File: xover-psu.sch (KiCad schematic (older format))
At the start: 46 parts, among them J1 Screw_Terminal_01x02, J2 Screw_Terminal_01x02, J3 Screw_Terminal_01x02, J4 Screw_Terminal_01x03, J5 Screw_Terminal_01x03, K1 RTE2xxxx, U1 LM317_3PinPackage, U2 LM337_TO220

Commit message: Added unmute-timing draft schematic (mostly FETs, untested)
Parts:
- removed K1: RTE2xxxx, Relay_THT:Relay_DPDT_Schrack-RT2-FormC_RM5mm, symbol Relay:RTE2xxxx
- added C1, C2: 100n, Capacitors_ThroughHole:C_Rect_L18.0mm_W6.0mm_P15.00mm_FKS3_FKP3, symbol Device:C
- added C11, C12: 1000u, Capacitors_ThroughHole:CP_Radial_D16.0mm_P7.50mm, symbol Device:CP
- added C15: 10u, Capacitors_SMD:C_0805, symbol Device:C
- added C3: 220u, Capacitors_SMD:CP_Elec_10x10, symbol Device:C
- added C4: 1u, Capacitors_SMD:C_0805, symbol Device:C
- added D1, D10, D23, D3, D5: LL4148, Diodes_SMD:D_MiniMELF, symbol Device:D
- added D11, D12, D15: M7, Diodes_SMD:D_SMA, symbol Device:D
- added D2, D20, D21, D22, D4: LED, LEDs:LED_0805, symbol Device:LED
- added F1, F2: 500mA, symbol Device:Fuse_Small
- added J2, J6, J7: Screw_Terminal_01x02, Terminals_Phoenix:TerminalBlock_Phoenix_MPT-2.54mm_2pol, symbol Connector:Screw_Terminal_01x02
- added K1: T9GS5L14-12, symbol Relay:RAYEX-L90S
- added L1: PM3700_70_RC, symbol Device:L_Coupled
- added PS1: HLK-10M12, Converter_ACDC:Converter_ACDC_HiLink_HLK-PMxx, symbol Converter_ACDC:HLK-PM12
- added Q1, Q5: AO3400, TO_SOT_Packages_SMD:SOT-23, symbol Device:Q_NMOS_GSD
- added Q2, Q3, Q4: 2N7002, TO_SOT_Packages_SMD:SOT-23, symbol Device:Q_NMOS_GSD
- added R1, R2, R20, R22, R24, R25, R5: 3k9, Resistors_SMD:R_0805, symbol Device:R
- added R10, R6: 47k, Resistors_SMD:R_0805, symbol Device:R
- added R11, R17: 470k, Resistors_SMD:R_0805, symbol Device:R
- added R12: 1k, Resistors_SMD:R_0805, symbol Device:R
- added R21, R3: 100, Resistors_SMD:R_0805, symbol Device:R
- added R23, R4, R7: 10k, Resistors_SMD:R_0805, symbol Device:R
- added RV1, RV2: 10D471K, Varistors:RV_Disc_D12_W3.9_P7.5, symbol Device:Varistor
- added U1, U4: 817C, Package_DIP:DIP-4_W7.62mm, symbol Isolator:PC817
- gave numbers to parts that had none: 2
- renumbered C6 to C10, C7 to C13, C8 to C14, C9 to C16, C10 to C17, C11 to C18, C12 to C19, C13 to C20, C14 to C21, C15 to C22, C16 to C23, C1 to C5, C2 to C6, C3 to C7, C4 to C8, C5 to C9, D5 to D13, D6 to D14, D7 to D16, D8 to D17, D9 to D18, D10 to D19, D1 to D6, D2 to D7, D3 to D8, D4 to D9, J2 to J3, J3 to J4, J4 to J5, J5 to J8, R1 to R13, R2 to R14, R3 to R15, R4 to R16, R5 to R18, R6 to R19, U1 to U2, U2 to U3
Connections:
- net labels added: 12V, AC1, AC2, AGND, DGND, RECT1, VCC, VEE
- net labels removed: GND
- wire segments 180 -> 331
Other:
- note added: "DC Control Supply\nAlways On"
- note added: "Line"
- note added: "Regulated\nOutput\n"
- note added: "Relay"
- note added: "Relay driver on 12V control supply"
- note added: "Remote"
- note added: "Turn-on Delay with Reset\n1s rise-time, fast turn-off\n"
- note added: "Turnoff-Detection\nFast Rise, 100ms fall"
- note added: "Unmute"
- note removed: "DC"
- note removed: "HV AC"
- note removed: "LV AC"
- note removed: "Remote On 12V"
- moved on the sheet: C13, C14, C16, C17, C18, C19, C20, C21, C22, C23, D13, D14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

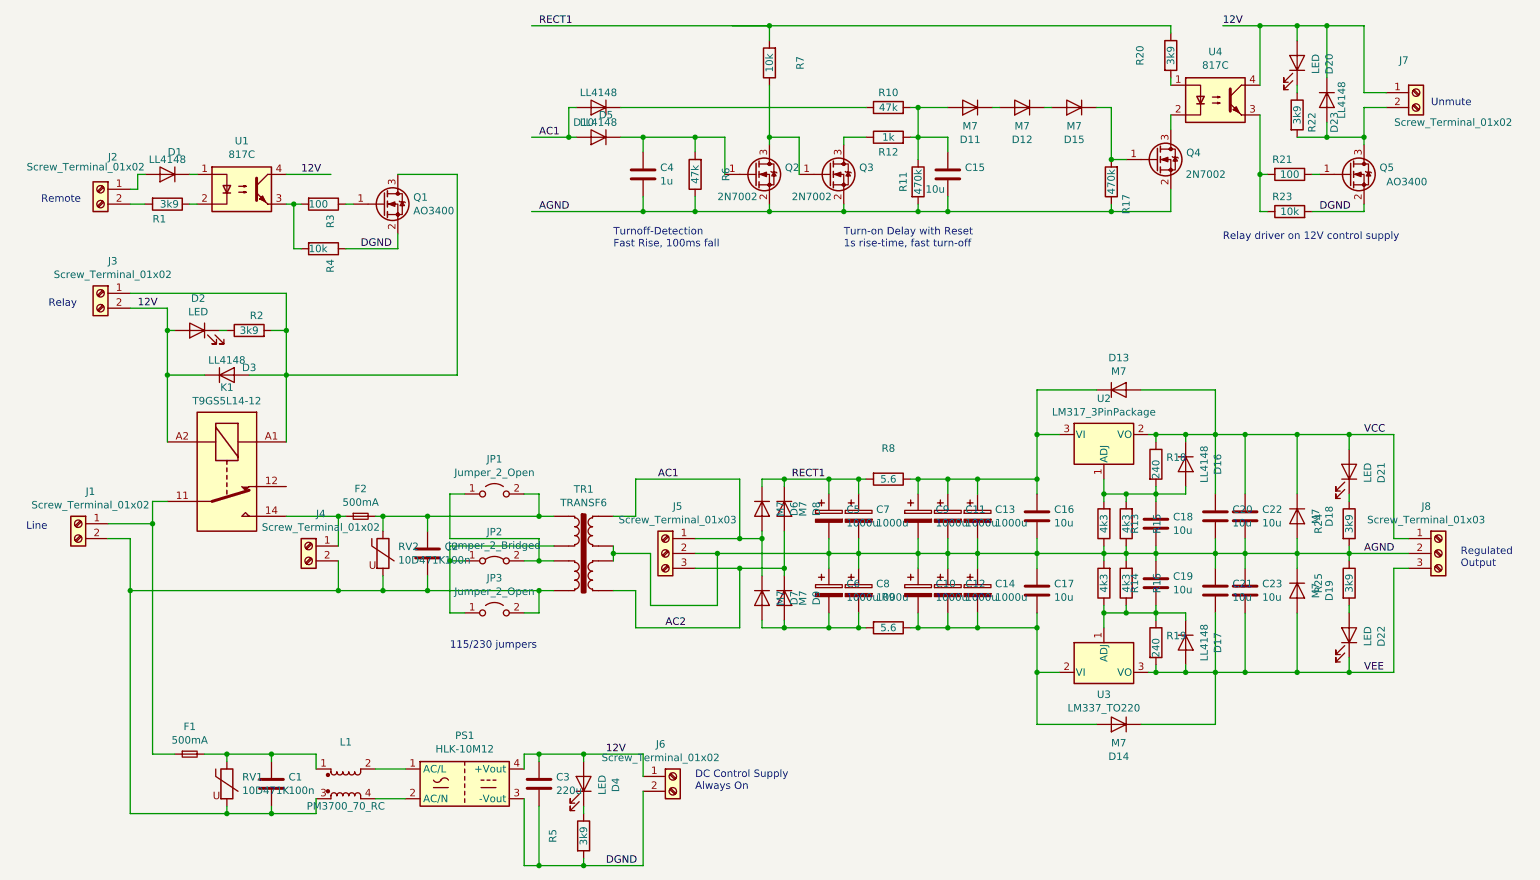
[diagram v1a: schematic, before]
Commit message: Converted unmute circuit to TL431 for distinct turn-on/off behaviour
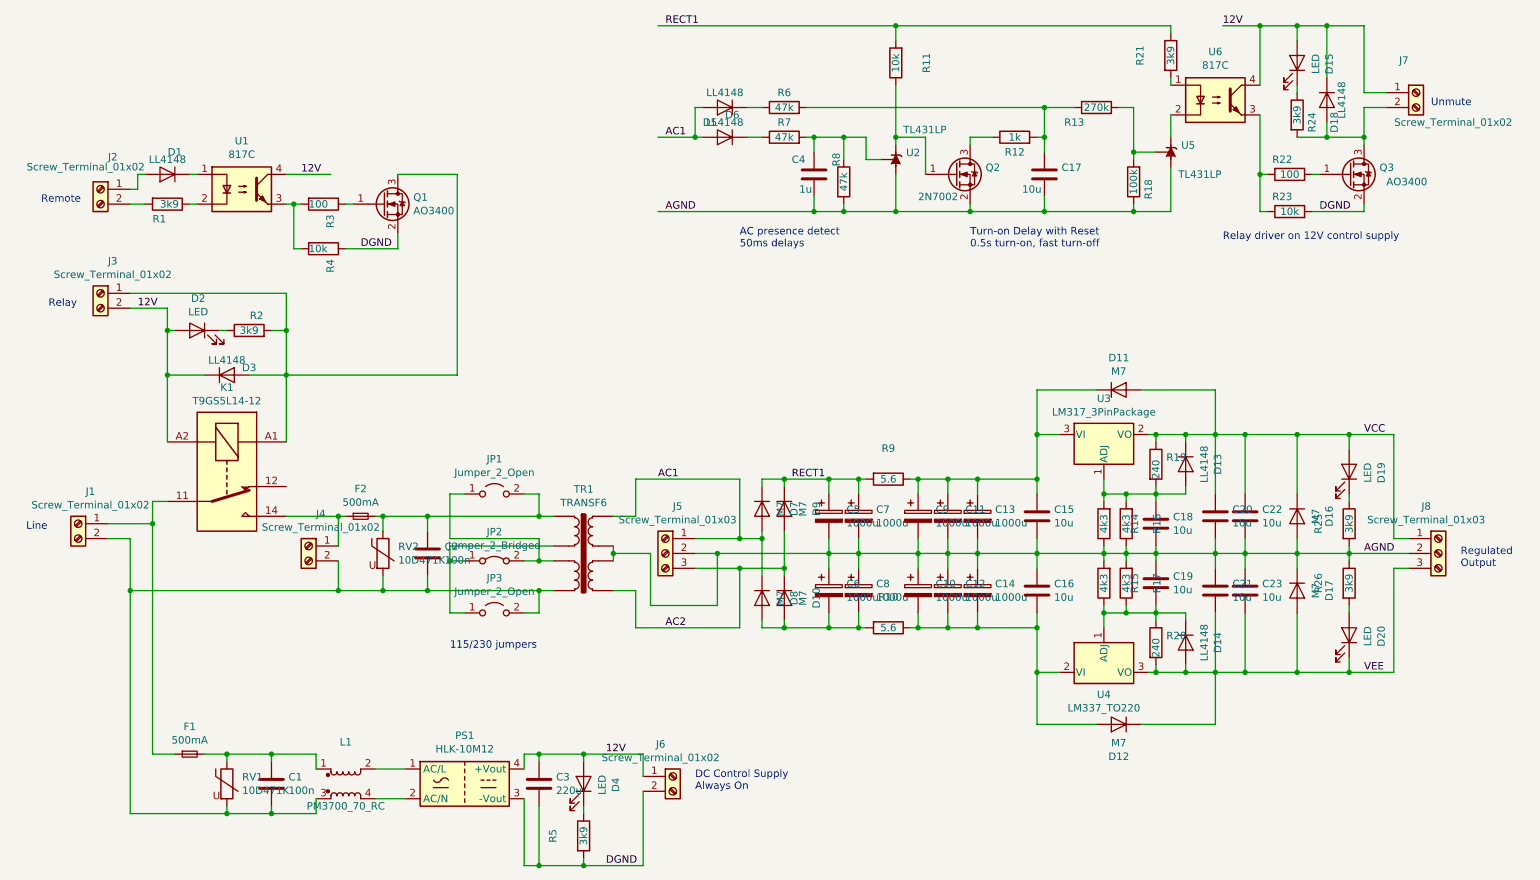
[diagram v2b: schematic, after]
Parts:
- removed D11, D12, D15: M7, Diodes_SMD:D_SMA, symbol Device:D
- removed Q2, Q4: 2N7002, TO_SOT_Packages_SMD:SOT-23, symbol Device:Q_NMOS_GSD
- removed R11: 470k, Resistors_SMD:R_0805, symbol Device:R
- added R13: 270k, Resistors_SMD:R_0805, symbol Device:R
- added R8: 47k, Resistors_SMD:R_0805, symbol Device:R
- added U2, U5: TL431LP, Package_TO_SOT_THT:TO-92_Inline, symbol Reference_Voltage:TL431LP
- R18: renamed from R17; value 470k -> 100k
- renumbered C16 to C15, C17 to C16, C15 to C17, D9 to D10, D13 to D11, D14 to D12, D16 to D13, D17 to D14, D20 to D15, D18 to D16, D19 to D17, D23 to D18, D21 to D19, D22 to D20, D10 to D5, D5 to D6, D6 to D7, D7 to D8, D8 to D9, Q3 to Q2, Q5 to Q3, R9 to R10, R7 to R11, R13 to R14, R14 to R15, R15 to R16, R16 to R17, R18 to R19, R19 to R20, R20 to R21, R21 to R22, R22 to R24, R24 to R25, R25 to R26, R10 to R6, R6 to R7, R8 to R9, U2 to U3, U3 to U4, U4 to U6
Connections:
- net AGND: now also R8.2, U2.2 (A), U5.2 (A); no longer R7.1
- net at C4.1, R7.2: now also R8.1, U2.1 (REF); no longer D6.1 (K)
- net at C17.1, R12.2, R6.2: now also R13.1
- net at Q2.1 (G), R11.1: now also U2.3 (K)
- net at R18.2: now also R13.2, U5.1 (REF)
- net at U6.2: now also U5.3 (K)
- new net: D6.1 (K), R7.1
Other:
- note added: "AC presence detect\n50ms delays"
- note added: "Turn-on Delay with Reset\n0.5s turn-on, fast turn-off\n"
- note removed: "Turn-on Delay with Reset\n1s rise-time, fast turn-off\n"
- note removed: "Turnoff-Detection\nFast Rise, 100ms fall"
- moved on the sheet: C17, C4, D5, D6, Q2, R11, R12, R18, R6, R7
